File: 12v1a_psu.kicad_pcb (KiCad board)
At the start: 2 copper layers, 18 parts, among them J1 AC_in, J2 P1, J3 P2, J4 Vout, Q1 BD440, SW1 SW_SPST, U1 LM7812

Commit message: Work on pcb layout
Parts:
- added REF**: Heatsink, Heatsink:Heatsink, F.Cu at (201.0, 70.0)
- added REF**: Heatsink, Heatsink:Heatsink, F.Cu at (201.0, 107.0)
- J1, J2, J3, SW1: footprint Connector_Wire:SolderWirePad_1x02_P7.62mm_Drill2.5mm -> Connector_Wire:SolderWirePad_1x02_P5.08mm_Drill1.5mm
- moved J2 80.8 mm to (100.9, 57.0)
- moved C2 71.8 mm to (198.0, 78.0), turned to 180 degrees
- moved SW1 63.5 mm to (119.1, 57.0), turned to 180 degrees
- moved U1 56.6 mm to (198.4, 73.3)
- moved J1 55.0 mm to (132.0, 57.0), turned to 180 degrees
- moved R2 49.8 mm to (195.0, 116.0)
- moved J3 45.6 mm to (140.0, 57.0)
- moved J4 44.3 mm to (162.0, 58.0), turned to 270 degrees
- moved D5 37.0 mm to (157.0, 121.0)
- moved D2 29.0 mm to (159.0, 109.0)
- moved D3 26.9 mm to (187.0, 102.0), turned to 180 degrees
- moved D4 26.9 mm to (187.0, 109.0), turned to 180 degrees
- moved C1 22.0 mm to (178.0, 80.0), turned to 180 degrees
- moved D1 21.8 mm to (159.0, 102.0)
- moved Q1 19.9 mm to (197.9, 109.0)
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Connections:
- TR1 pad 2: Net-(TR1-Pad2) -> Net-(J2-Pad2)
- TR1 pad 3: Net-(TR1-Pad3) -> Net-(J3-Pad1)

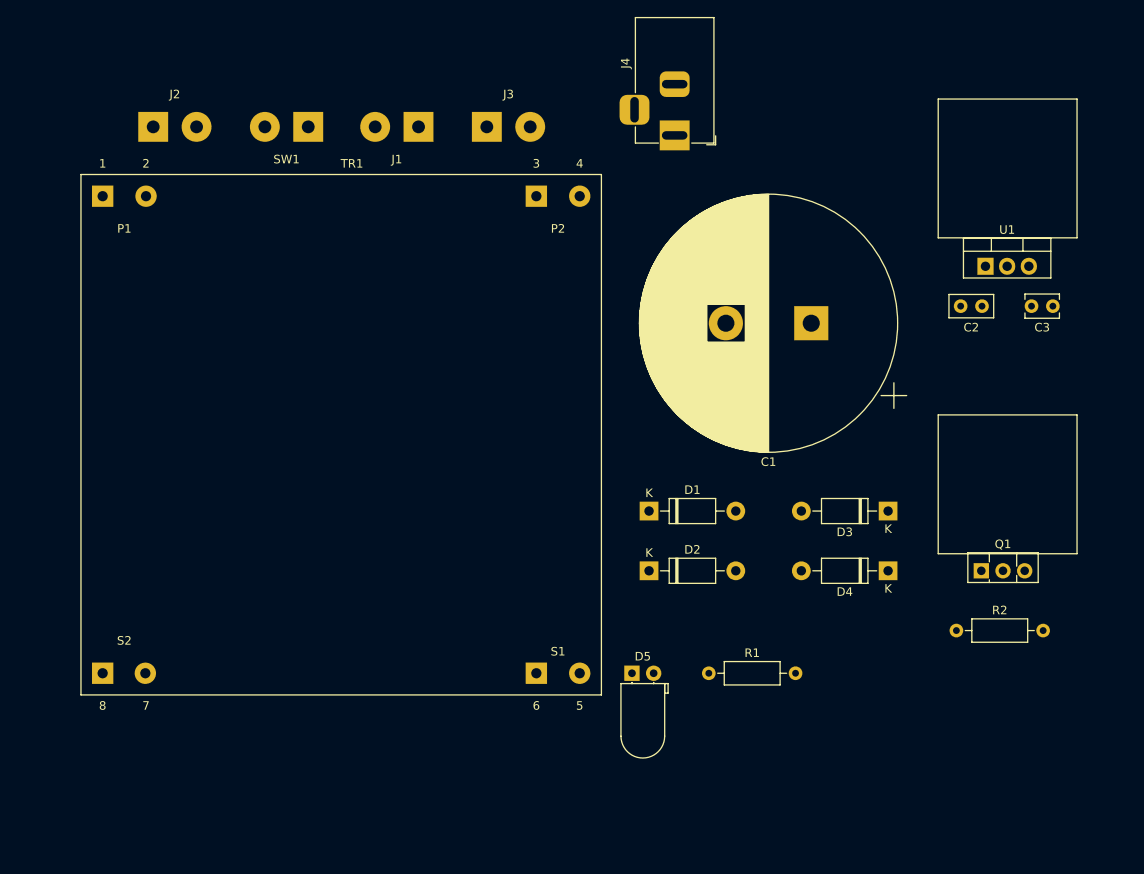
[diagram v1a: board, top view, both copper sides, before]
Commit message: reorganize and finalize board size
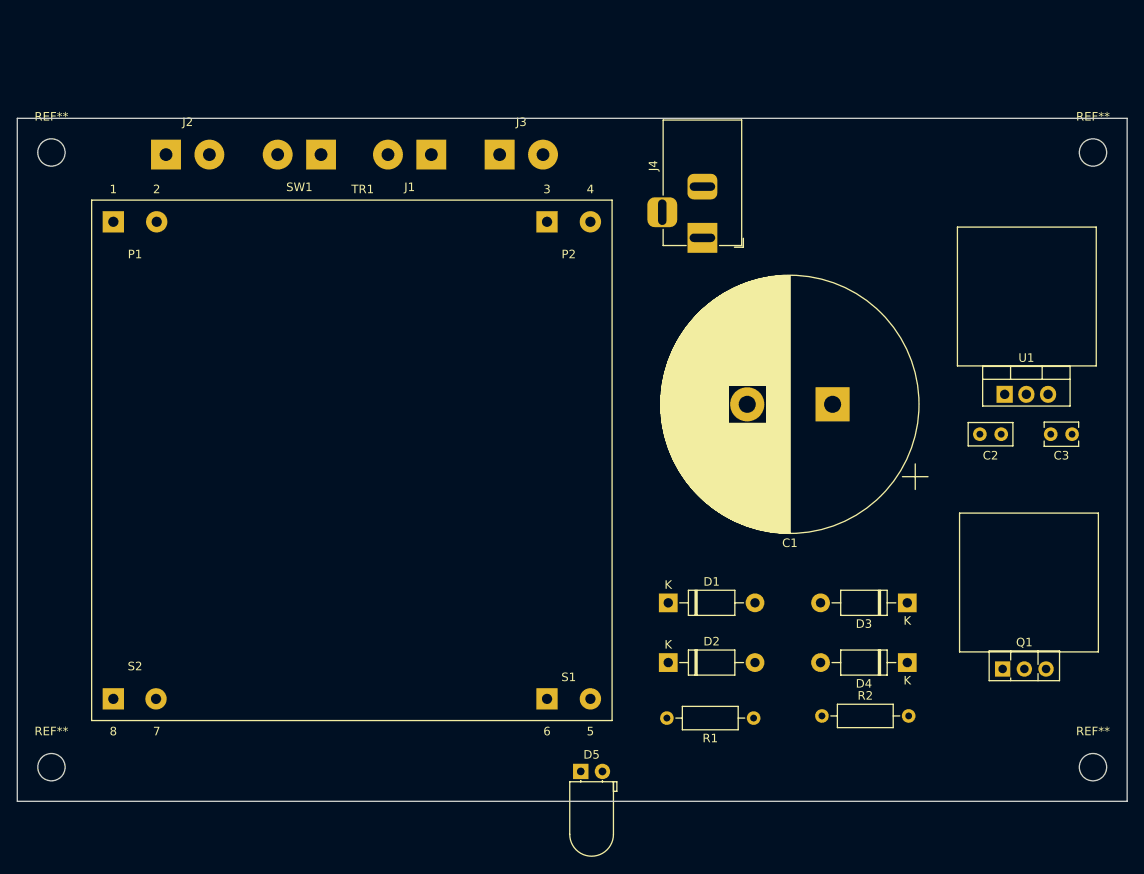
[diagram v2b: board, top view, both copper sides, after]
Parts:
- added REF**: MountingHole_3.2mm_M3, MountingHole:MountingHole_3.2mm_M3, F.Cu at (89.0, 132.0)
- added REF**: MountingHole_3.2mm_M3, MountingHole:MountingHole_3.2mm_M3, F.Cu at (211.0, 60.0)
- added REF**: MountingHole_3.2mm_M3, MountingHole:MountingHole_3.2mm_M3, F.Cu at (211.0, 132.0)
- added REF**: MountingHole_3.2mm_M3, MountingHole:MountingHole_3.2mm_M3, F.Cu at (89.0, 60.0)
- moved R2 18.7 mm to (179.2, 126.0)
- moved C2 15.2 mm to (200.2, 93.0)
- moved C3 15.2 mm to (206.1, 93.0)
- moved REF** 15.2 mm to (203.2, 85.0)
- moved U1 15.2 mm to (200.7, 88.3)
- moved D5 13.0 mm to (151.0, 132.5)
- moved J4 12.4 mm to (165.2, 70.0)
- moved Q1 11.8 mm to (200.4, 120.5)
- moved REF** 11.8 mm to (203.5, 118.5)
- moved D1 11.0 mm to (161.2, 112.8)
- moved D2 11.0 mm to (161.2, 119.8)
- moved D3 11.0 mm to (189.2, 112.8)
- moved D4 11.0 mm to (189.2, 119.8)
- moved C1 9.82 mm to (180.5, 89.5)
- moved R1 7.42 mm to (171.2, 126.2), turned to 180 degrees
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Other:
- board outline added: 130 x 80 mm

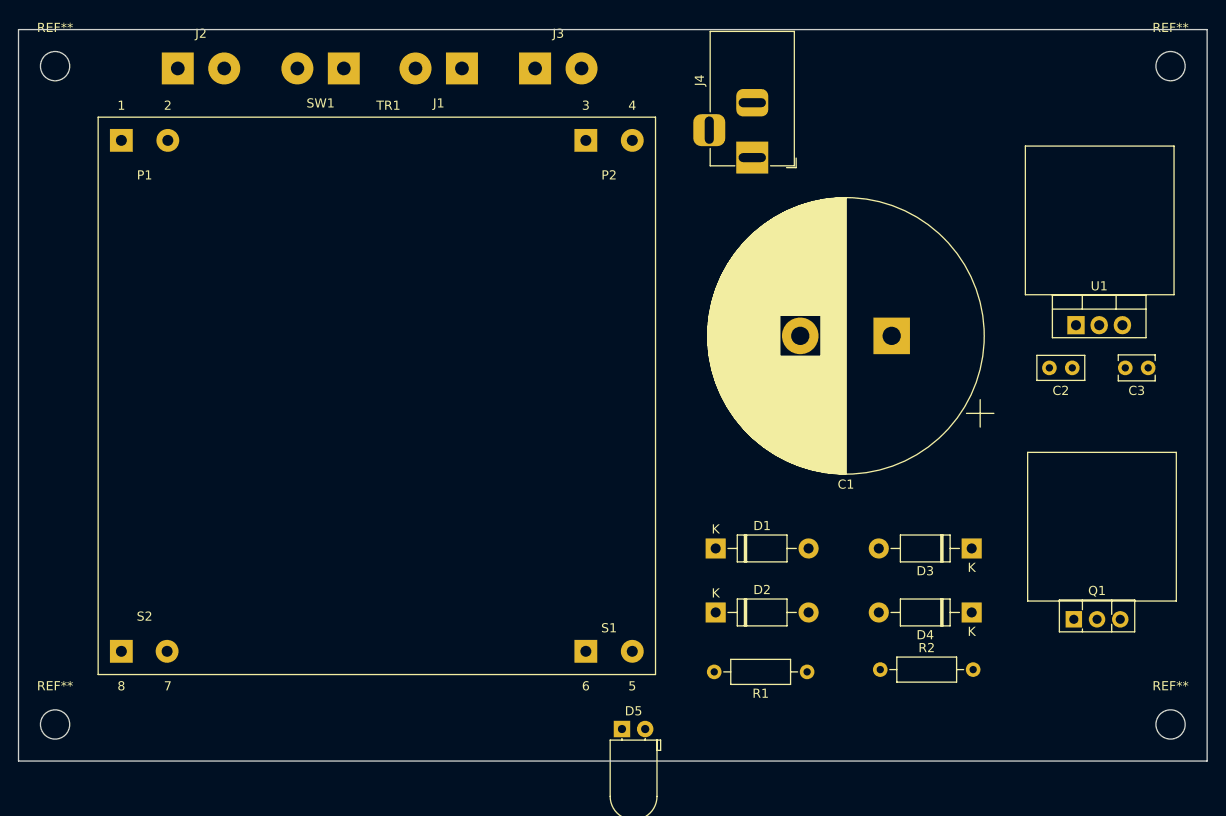
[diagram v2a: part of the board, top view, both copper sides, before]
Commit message: Add traces and ground plane
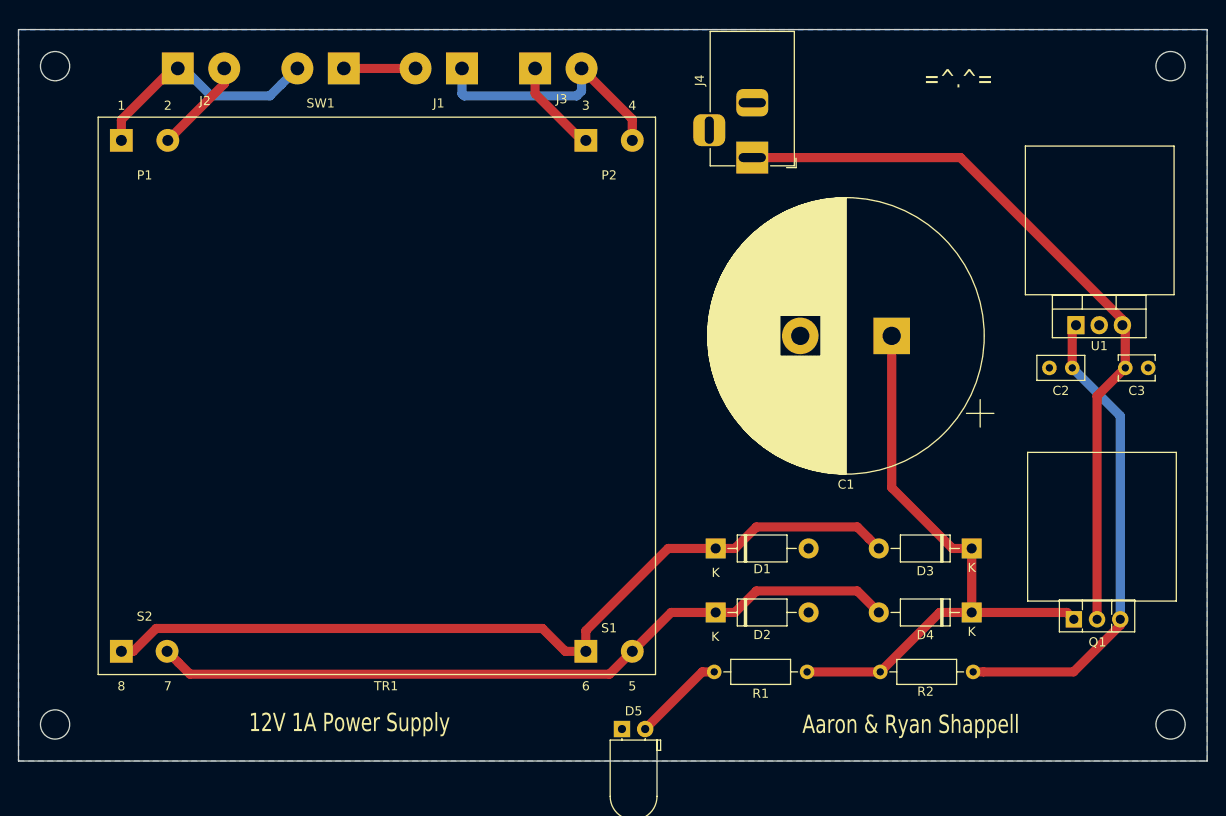
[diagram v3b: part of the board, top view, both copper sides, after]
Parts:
- moved R2 0.25 mm to (179.2, 126.2)
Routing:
- net /S1P: track 0.00 -> 92.8 mm
- net /S1N: track 0.00 -> 83.6 mm
- net Net-(C3-Pad1): track 0.00 -> 82.0 mm
- net Net-(C1-Pad1): track 0.00 -> 67.3 mm
- net Net-(C2-Pad1): track 0.00 -> 53.4 mm
- net Net-(J1-Pad1): track 0.00 -> 28.8 mm
- net Net-(J2-Pad1): track 0.00 -> 26.3 mm
- net Net-(J2-Pad2): track 0.00 -> 10.4 mm
- net Net-(J3-Pad1): track 0.00 -> 10.4 mm
- net Net-(D5-Pad2): track 0.00 -> 10.1 mm
- net Net-(J1-Pad2): track 0.00 -> 7.84 mm
- added copper zone on B.Cu, net GND
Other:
- net class Default: clearance 0.2 -> 0.75; trace_width 0.25 -> 1
- rule trace_clearance: 0.2 -> 0.75
- board text added: "12V 1A Power Supply"
- board text added: "=^.^="
- board text added: "Aaron & Ryan Shappell"

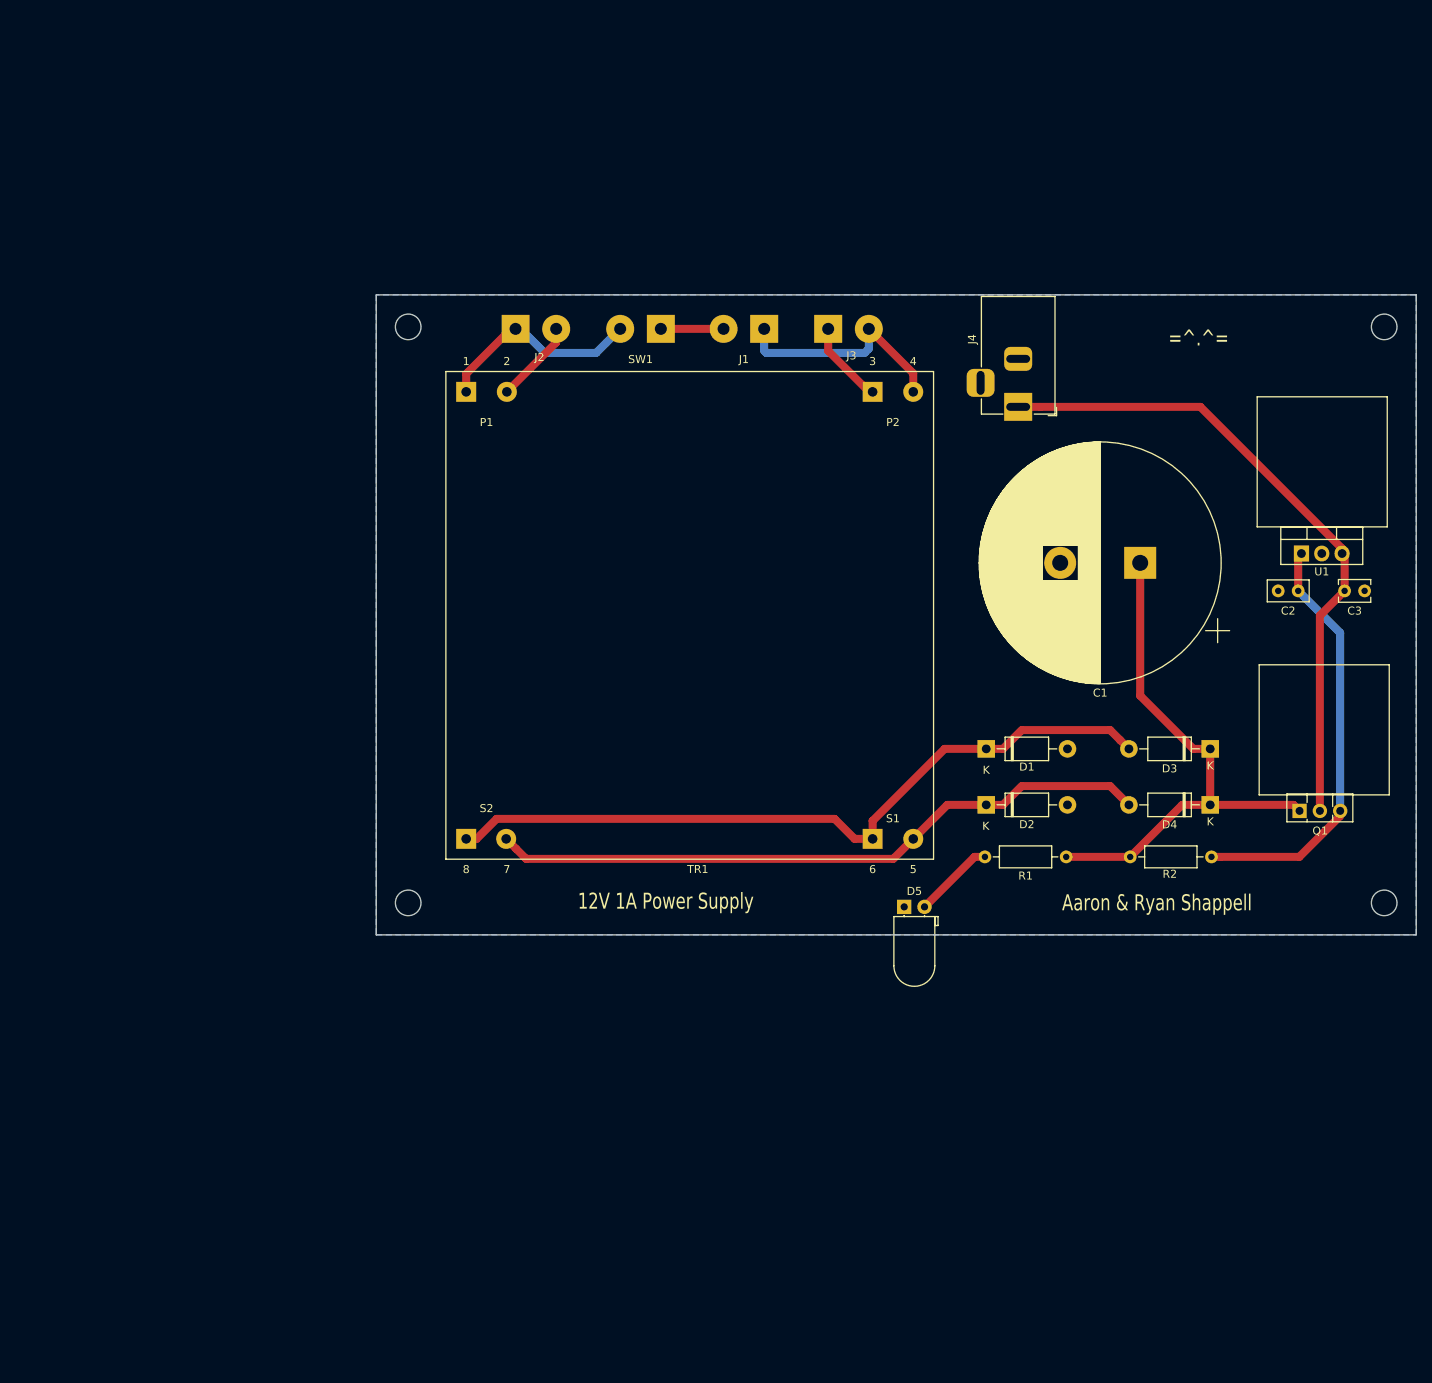
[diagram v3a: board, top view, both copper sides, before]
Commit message: Resize board for switch and ac input
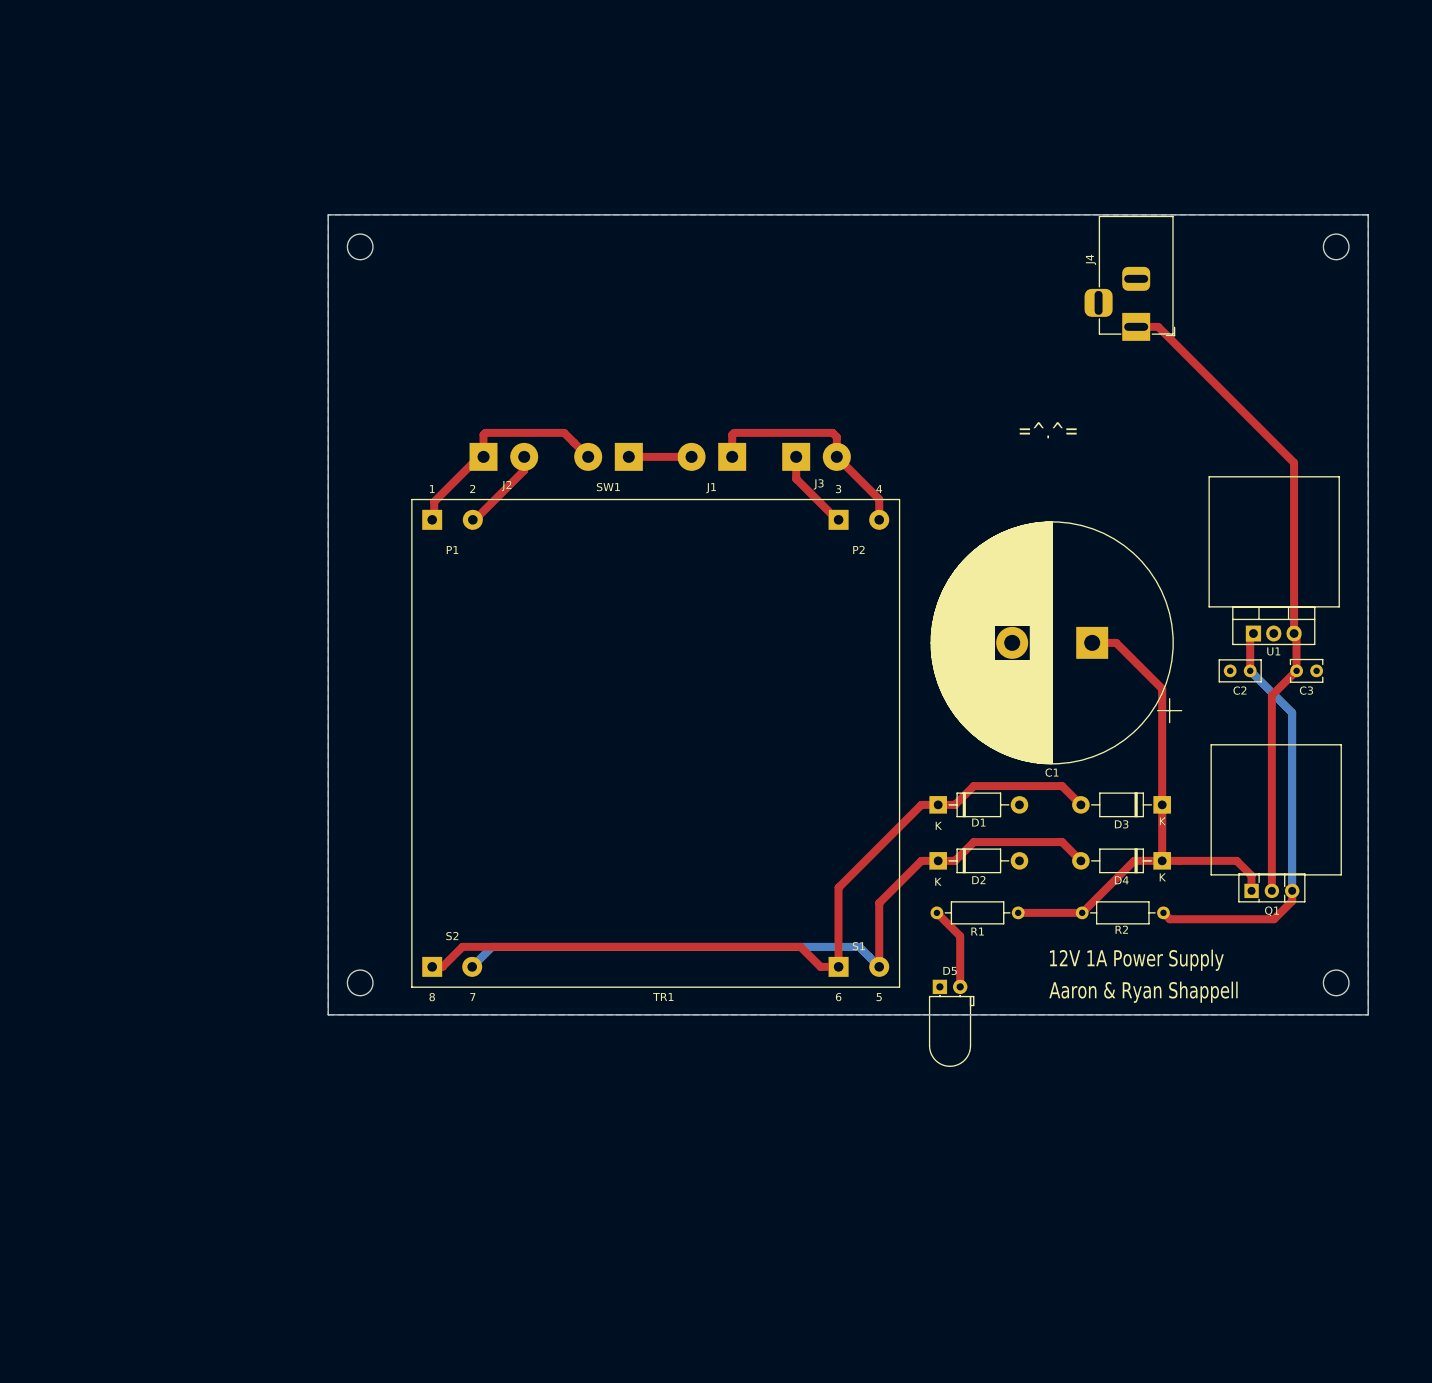
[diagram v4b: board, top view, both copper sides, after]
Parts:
- moved J4 17.8 mm to (180.0, 60.0)
- moved TR1 16.6 mm to (92.0, 140.0)
- moved J1 16.5 mm to (129.5, 76.2)
- moved J2 16.5 mm to (98.4, 76.2)
- moved J3 16.5 mm to (137.5, 76.2)
- moved SW1 16.5 mm to (116.6, 76.2)
- moved C1 11.7 mm to (174.5, 99.5)
- moved C2 11.7 mm to (194.2, 103.0)
- moved C3 11.7 mm to (200.1, 103.0)
- moved Q1 11.7 mm to (194.4, 130.5)
- moved REF** 11.7 mm to (83.0, 142.0)
- moved REF** 11.7 mm to (205.0, 50.0)
- moved REF** 11.7 mm to (205.0, 142.0)
- moved REF** 11.7 mm to (83.0, 50.0)
- moved REF** 11.7 mm to (197.2, 95.0)
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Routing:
- net /S1N: track 83.6 -> 90.3 mm
- net /S1P: track 92.8 -> 99.3 mm
- net Net-(J2-Pad1): track 26.3 -> 28.6 mm
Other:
- board size 130 x 80 mm -> 130 x 100 mm

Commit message: add graphic and small adjustments
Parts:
- moved C1 7.90 mm to (174.4, 91.6)
- moved C3 6.40 mm to (199.8, 96.6)
- moved C2 6.40 mm to (194.1, 96.6)
- moved REF** 6.40 mm to (197.1, 88.6)
- moved U1 6.40 mm to (194.5, 91.9)
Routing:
- net Net-(C1-Pad1): track 67.2 -> 76.3 mm
- net Net-(C2-Pad1): track 53.2 -> 59.0 mm
